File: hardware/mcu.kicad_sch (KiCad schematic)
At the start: 19 parts, among them J1 Micro_SD_Card, J3 USB_C_Receptacle_USB2.0_14P, Q1 Q_NPN_BEC, Q2 Q_NPN_BEC, U1 ESP32-S3-WROOM-1, U6 CH340G

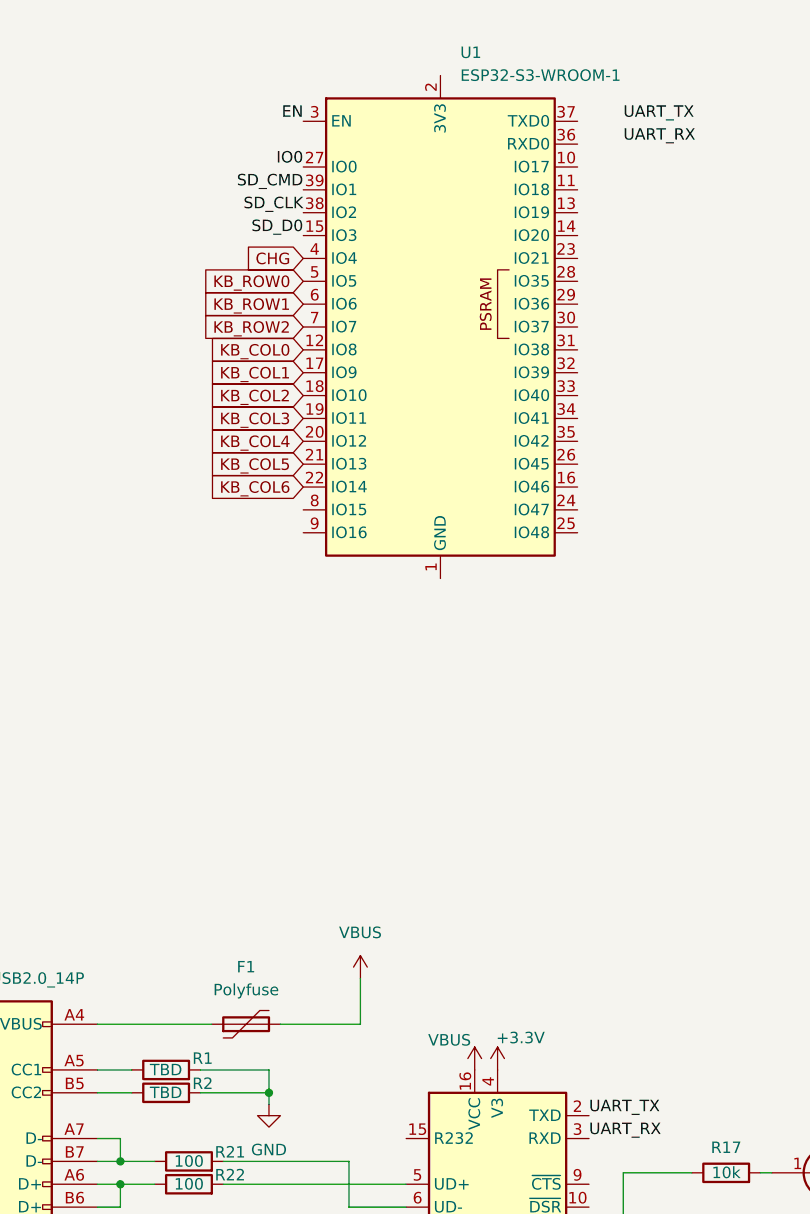
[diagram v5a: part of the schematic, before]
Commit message: rename power symbols, power switch on EN pin instead of VIN
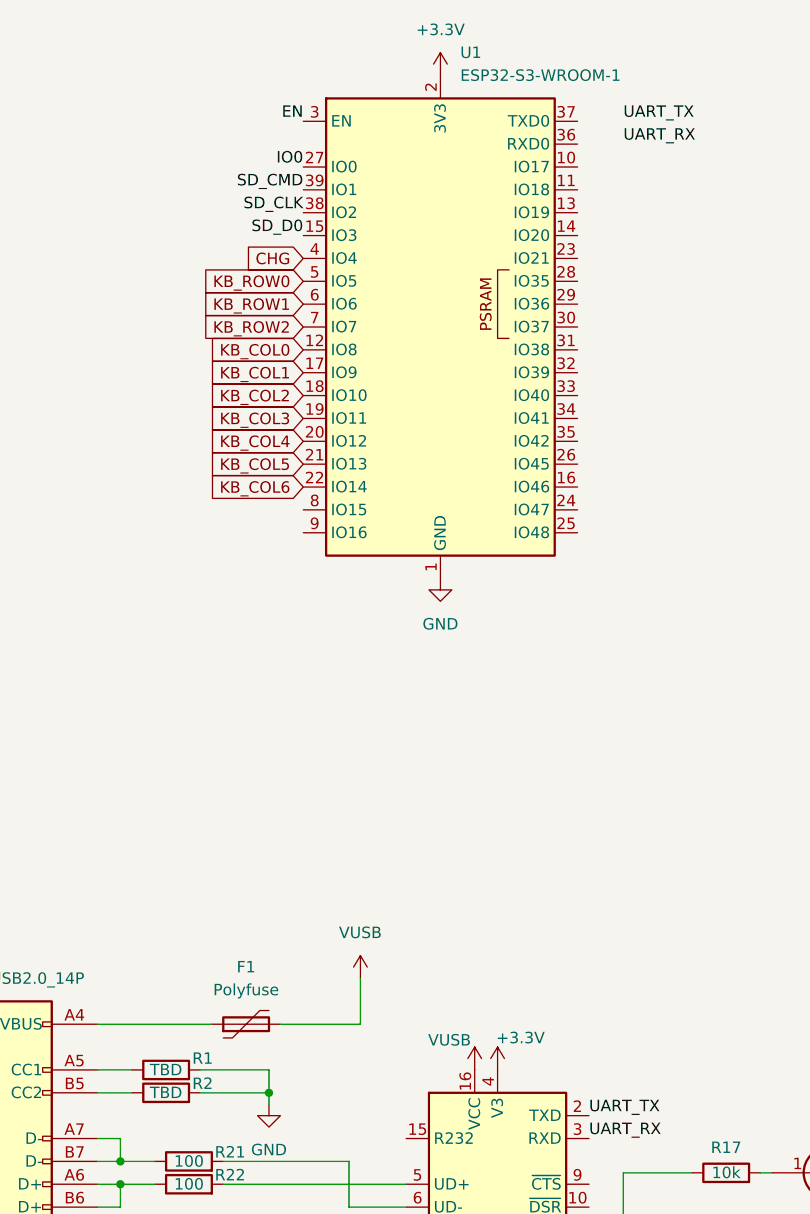
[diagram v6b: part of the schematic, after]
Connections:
- net +3.3V: now also U1.2 (3V3)
- net GND: now also U1.1 (GND), U1.40 (GND), U1.41 (GND)
- net VBUS renamed VUSB
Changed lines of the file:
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@@
+	)
+	(symbol
+		(lib_id "power:+3.3V")
+		(at 86.36 38.1 0)
+		(unit 1)
+		(exclude_from_sim no)
+		(in_bom yes)
+		(on_board yes)
+		(dnp no)
+		(fields_autoplaced yes)
+		(property "Reference" "#PWR045"
+			(at 86.36 41.91 0)
+			(effects
+				(font
+					(size 1.27 1.27)
+				)
+				(hide yes)
+			)
+		)
+		(property "Value" "+3.3V"
+			(at 86.36 33.02 0)
+			(effects
+				(font
+					(size 1.27 1.27)
+				)
+			)
+		)
+		(property "Footprint" ""
+			(at 86.36 38.1 0)
+			(effects
+				(font
+					(size 1.27 1.27)
+				)
+				(hide yes)
+			)
+		)
+		(property "Datasheet" ""
+			(at 86.36 38.1 0)
+			(effects
+				(font
+					(size 1.27 1.27)
+				)
+				(hide yes)
+			)
+		)
+		(property "Description" "Power symbol creates a global label with name \"+3.3V\""
+			(at 86.36 38.1 0)
+			(effects
+				(font
+					(size 1.27 1.27)
+				)
+				(hide yes)
+			)
+		)
+		(pin "1"
+		)
+		(instances
+			(project "badge"
+				(path "/dc4a3d77-b0f8-4e90-a4be-3e93c7025348/d3fb9833-a00e-444d-9e5a-c108fd26b22a"
+					(reference "#PWR045")
+					(unit 1)
+				)
+			)
+		)
 	)
 	(symbol
@@
 			)
 		)
-		(property "Value" "VBUS"
+		(property "Value" "VUSB"
 			(at 87.376 145.288 0)
 			(effects
@@
 			)
 		)
-		(property "Value" "VBUS"
+		(property "Value" "VUSB"
 			(at 77.47 133.35 0)
 			(effects
@@
 					(unit 1)
 				)
+			)
+		)
+	)
+	(symbol
+		(lib_id "power:GND")
+		(at 86.36 93.98 0)
+		(unit 1)
+		(exclude_from_sim no)
+		(in_bom yes)
+		(on_board yes)
+		(dnp no)
+		(fields_autoplaced yes)
+		(property "Reference" "#PWR046"
+			(at 86.36 100.33 0)
+			(effects
+				(font
+					(size 1.27 1.27)
+				)
+				(hide yes)
+			)
+		)
+		(property "Value" "GND"
+			(at 86.36 99.06 0)
+			(effects
+				(font
+					(size 1.27 1.27)
+				)
+			)
+		)
+		(property "Footprint" ""
+			(at 86.36 93.98 0)
+			(effects
+				(font
+					(size 1.27 1.27)
+				)
+				(hide yes)
+			)
+		)
+		(property "Datasheet" ""
+			(at 86.36 93.98 0)
+			(effects
+				(font
+					(size 1.27 1.27)
+				)
+				(hide yes)
+			)
+		)
+		(property "Description" "Power symbol creates a global label with name \"GND\" , ground"
+			(at 86.36 93.98 0)
+			(effects
+				(font
+					(size 1.27 1.27)
+				)
+				(hide yes)
+			)
+		)
+		(pin "1"
+		)
+		(instances
+			(project "badge"
+				(path "/dc4a3d77-b0f8-4e90-a4be-3e93c7025348/d3fb9833-a00e-444d-9e5a-c108fd26b22a"
+					(reference "#PWR046")
+					(unit 1)
+				)

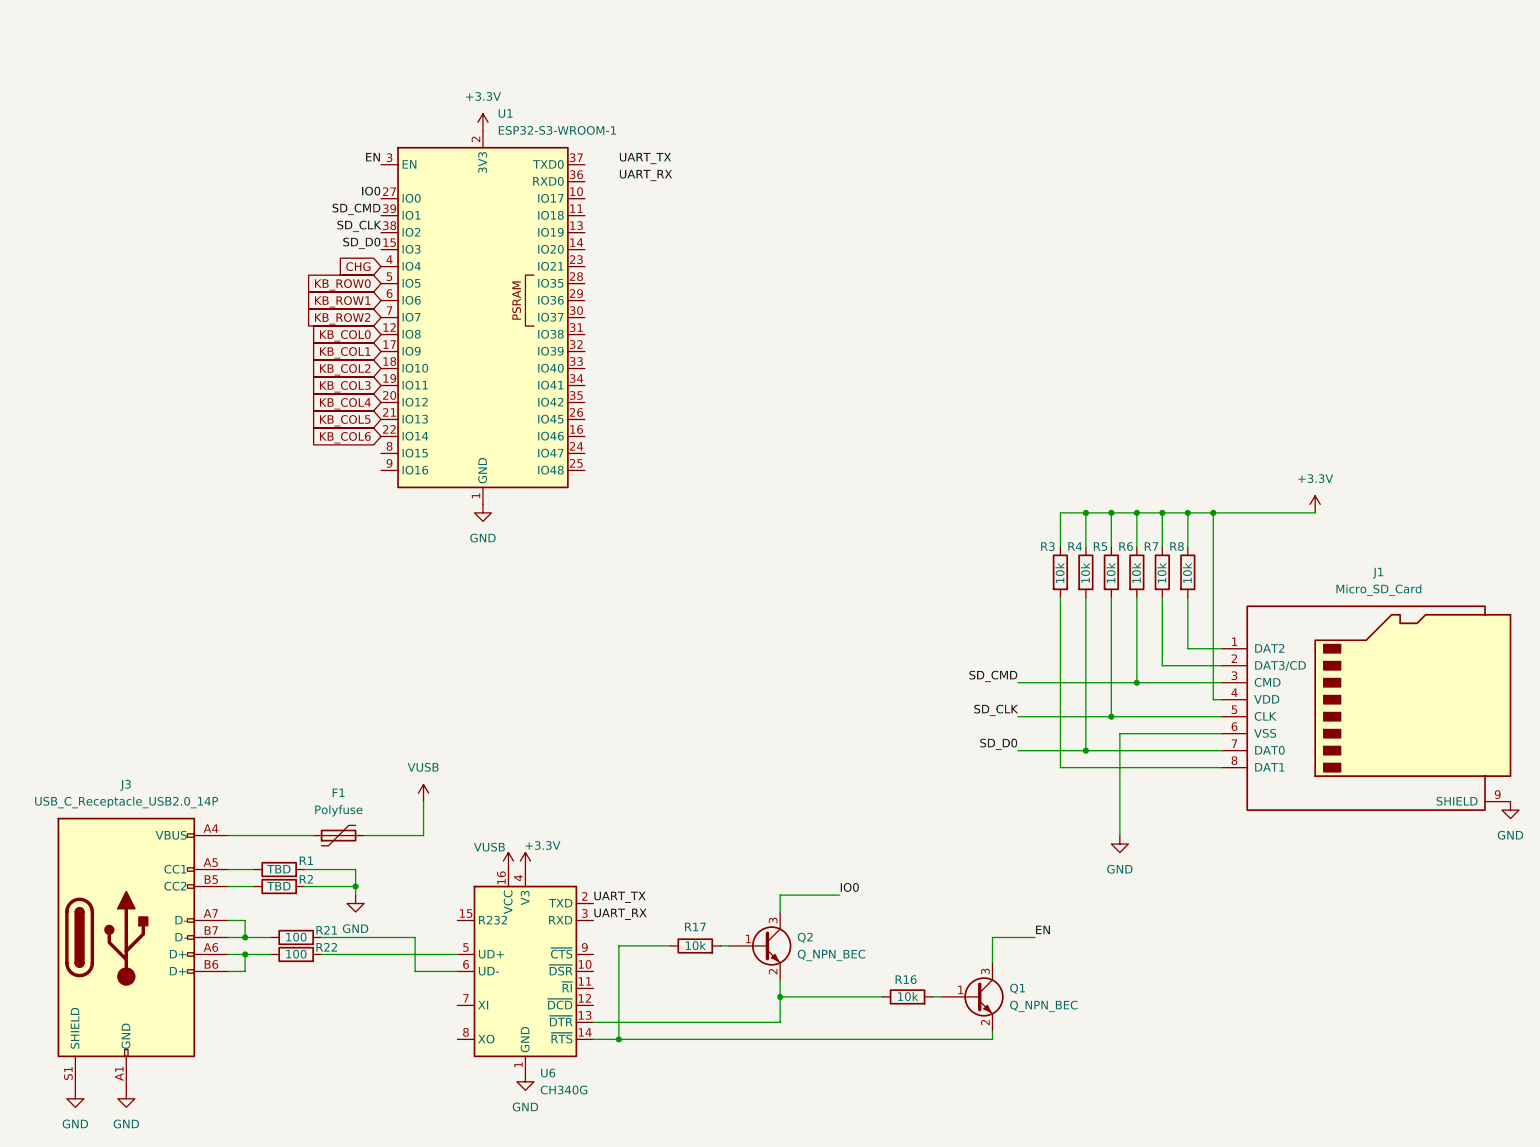
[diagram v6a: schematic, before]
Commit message: remove ch340
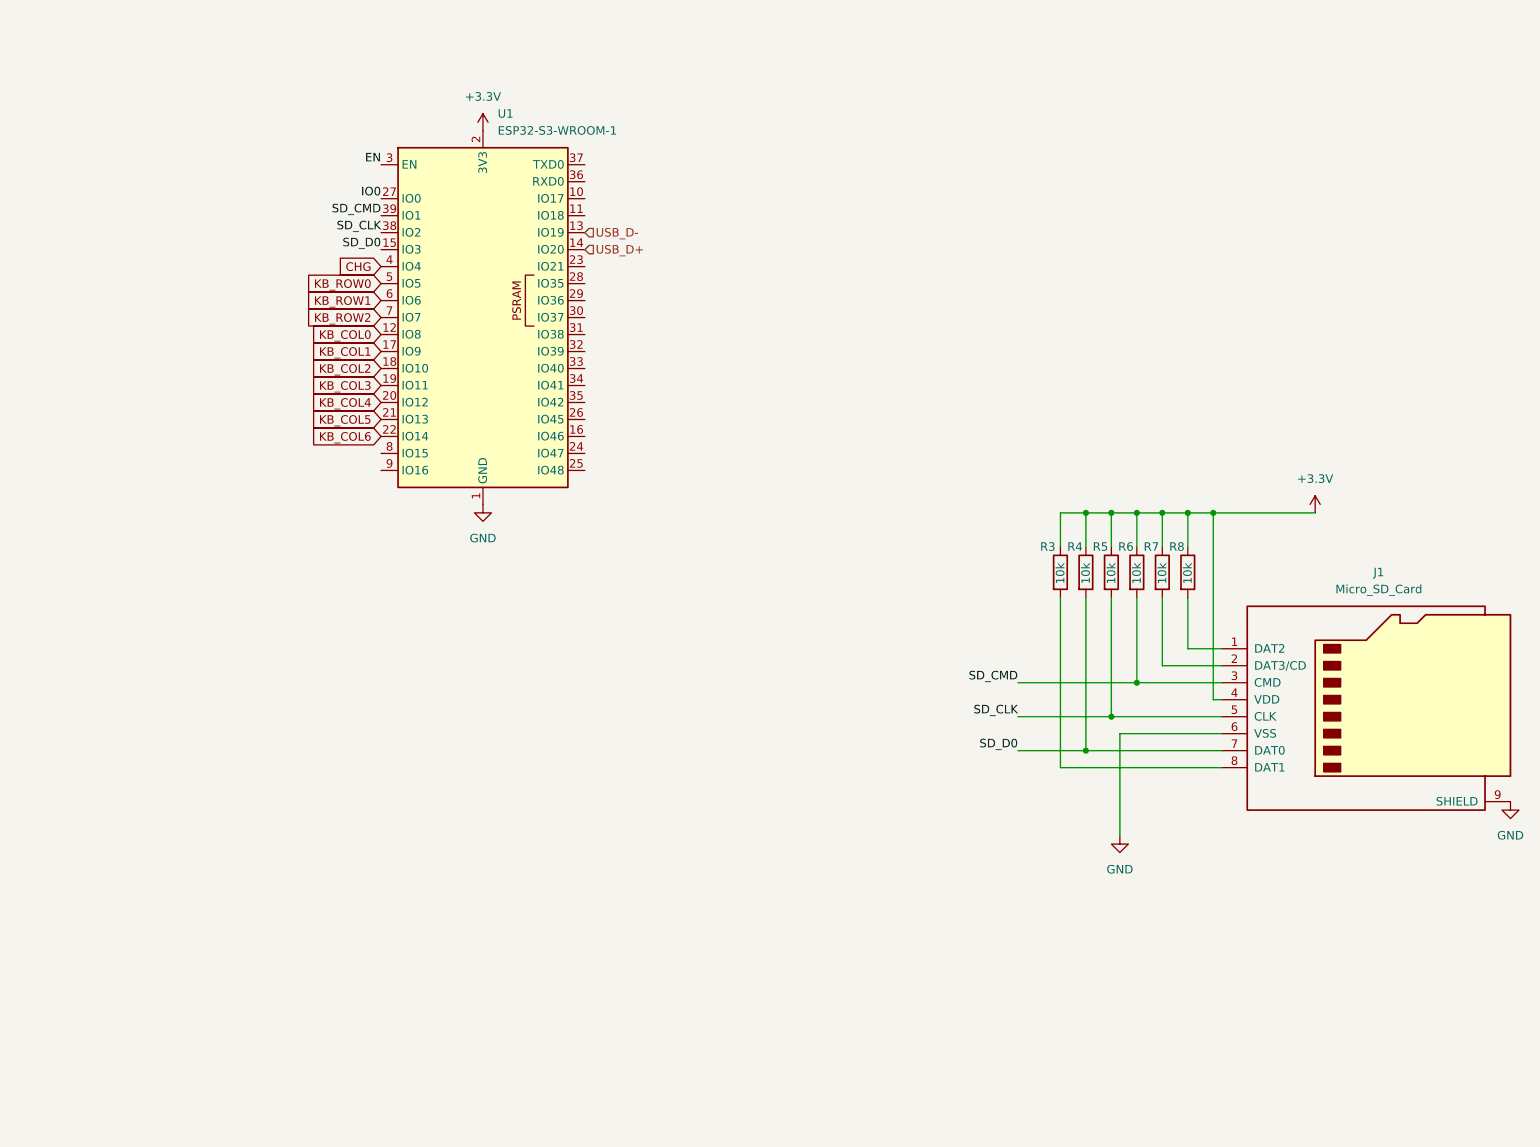
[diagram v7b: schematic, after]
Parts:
- removed F1: Polyfuse, symbol Device:Polyfuse
- removed J3: USB_C_Receptacle_USB2.0_14P, Connector_USB:USB_C_Receptacle_GCT_USB4105-xx-A_16P_TopMnt_Horizontal, symbol Connector:USB_C_Receptacle_USB2.0_14P
- removed Q1, Q2: Q_NPN_BEC, symbol Device:Q_NPN_BEC
- removed R1, R2: TBD, Resistor_SMD:R_0201_0603Metric, symbol Device:R
- removed R16, R17: 10k, symbol Device:R
- removed R21, R22: 100, Resistor_SMD:R_0201_0603Metric, symbol Device:R
- removed U6: CH340G, Package_SO:SOIC-16_3.9x9.9mm_P1.27mm, symbol Interface_USB:CH340G
- R3, R4, R5, R6, R7, R8: footprint Resistor_SMD:R_0201_0603Metric -> Resistor_SMD:R_0603_1608Metric
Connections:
- net USB_D-: now reaches U1.13 (IO19)
- net USB_D+: now reaches U1.14 (IO20)

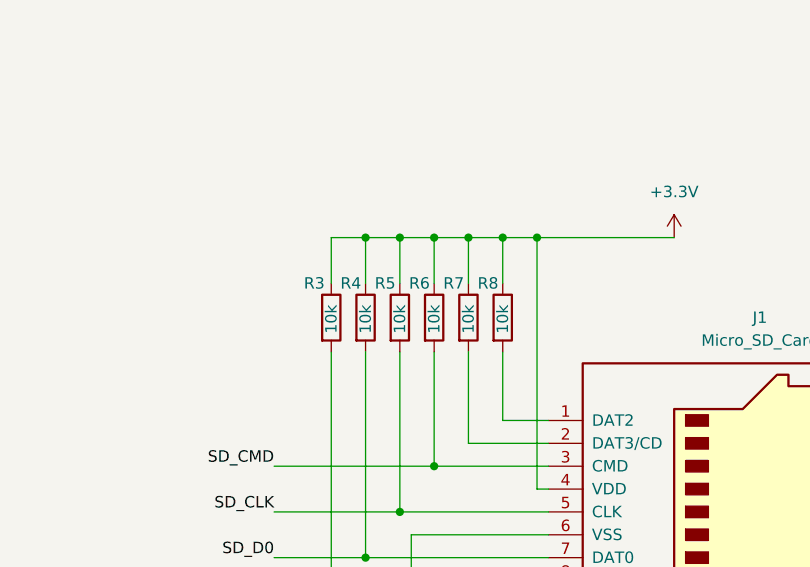
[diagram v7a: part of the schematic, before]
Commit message: update usb port, esd, lcsc
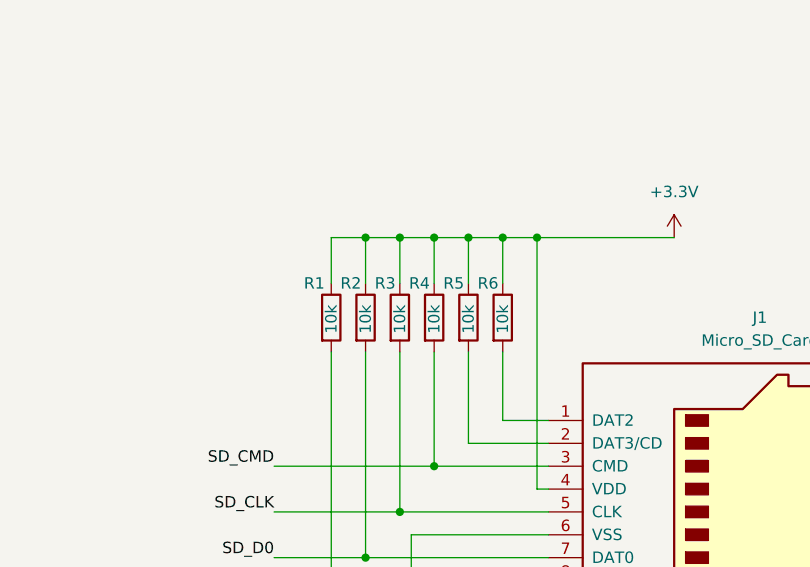
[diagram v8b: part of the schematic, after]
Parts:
- renumbered R3 to R1, R4 to R2, R5 to R3, R6 to R4, R7 to R5, R8 to R6
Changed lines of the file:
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@@
 		(dnp no)
 		(fields_autoplaced yes)
-		(property "Reference" "R3"
+		(property "Reference" "R1"
 			(at 169.672 100.33 0)
 			(effects
@@
 			(project "badge"
 				(path "/dc4a3d77-b0f8-4e90-a4be-3e93c7025348/d3fb9833-a00e-444d-9e5a-c108fd26b22a"
-					(reference "R3")
+					(reference "R1")
 					(unit 1)
 				)
@@
 		(dnp no)
 		(fields_autoplaced yes)
-		(property "Reference" "#PWR07"
+		(property "Reference" "#PWR05"
 			(at 240.03 144.78 0)
 			(effects
@@
 			(project "badge"
 				(path "/dc4a3d77-b0f8-4e90-a4be-3e93c7025348/d3fb9833-a00e-444d-9e5a-c108fd26b22a"
-					(reference "#PWR07")
+					(reference "#PWR05")
 					(unit 1)
 				)
@@
 		(dnp no)
 		(fields_autoplaced yes)
-		(property "Reference" "#PWR045"
+		(property "Reference" "#PWR01"
 			(at 86.36 41.91 0)
 			(effects
@@
 			(project "badge"
 				(path "/dc4a3d77-b0f8-4e90-a4be-3e93c7025348/d3fb9833-a00e-444d-9e5a-c108fd26b22a"
-					(reference "#PWR045")
+					(reference "#PWR01")
 					(unit 1)
 				)
@@
 		(dnp no)
 		(fields_autoplaced yes)
-		(property "Reference" "R4"
+		(property "Reference" "R2"
 			(at 173.736 100.33 0)
 			(effects
@@
 			(project "badge"
 				(path "/dc4a3d77-b0f8-4e90-a4be-3e93c7025348/d3fb9833-a00e-444d-9e5a-c108fd26b22a"
-					(reference "R4")
+					(reference "R2")
 					(unit 1)
 				)
@@
 		(dnp no)
 		(fields_autoplaced yes)
-		(property "Reference" "#PWR06"
+		(property "Reference" "#PWR03"
 			(at 181.61 149.86 0)
 			(effects
@@
 			(project "badge"
 				(path "/dc4a3d77-b0f8-4e90-a4be-3e93c7025348/d3fb9833-a00e-444d-9e5a-c108fd26b22a"
-					(reference "#PWR06")
+					(reference "#PWR03")
 					(unit 1)
 				)
@@
 		(dnp no)
 		(fields_autoplaced yes)
-		(property "Reference" "R8"
+		(property "Reference" "R6"
 			(at 188.976 100.33 0)
 			(effects
@@
 			(project "badge"
 				(path "/dc4a3d77-b0f8-4e90-a4be-3e93c7025348/d3fb9833-a00e-444d-9e5a-c108fd26b22a"
-					(reference "R8")
+					(reference "R6")
 					(unit 1)
 				)
@@
 		(dnp no)
 		(fields_autoplaced yes)
-		(property "Reference" "R7"
+		(property "Reference" "R5"
 			(at 185.166 100.33 0)
 			(effects
@@
 			(project "badge"
 				(path "/dc4a3d77-b0f8-4e90-a4be-3e93c7025348/d3fb9833-a00e-444d-9e5a-c108fd26b22a"
-					(reference "R7")
+					(reference "R5")
 					(unit 1)
 				)
@@
 		(dnp no)
 		(fields_autoplaced yes)
-		(property "Reference" "R5"
+		(property "Reference" "R3"
 			(at 177.546 100.33 0)
 			(effects
@@
 			(project "badge"
 				(path "/dc4a3d77-b0f8-4e90-a4be-3e93c7025348/d3fb9833-a00e-444d-9e5a-c108fd26b22a"
-					(reference "R5")
+					(reference "R3")
 					(unit 1)
 				)
@@
 		(dnp no)
 		(fields_autoplaced yes)
-		(property "Reference" "R6"
+		(property "Reference" "R4"
 			(at 181.356 100.33 0)
 			(effects
@@
 			(project "badge"
 				(path "/dc4a3d77-b0f8-4e90-a4be-3e93c7025348/d3fb9833-a00e-444d-9e5a-c108fd26b22a"
-					(reference "R6")
+					(reference "R4")
 					(unit 1)
 				)
@@
 		(dnp no)
 		(fields_autoplaced yes)
-		(property "Reference" "#PWR05"
+		(property "Reference" "#PWR04"
 			(at 210.82 99.06 0)
 			(effects
@@
 			(project "badge"
 				(path "/dc4a3d77-b0f8-4e90-a4be-3e93c7025348/d3fb9833-a00e-444d-9e5a-c108fd26b22a"
-					(reference "#PWR05")
+					(reference "#PWR04")
 					(unit 1)
 				)
@@
 		(dnp no)
 		(fields_autoplaced yes)
-		(property "Reference" "#PWR046"
+		(property "Reference" "#PWR02"
 			(at 86.36 100.33 0)
 			(effects
@@
 			(project "badge"
 				(path "/dc4a3d77-b0f8-4e90-a4be-3e93c7025348/d3fb9833-a00e-444d-9e5a-c108fd26b22a"
-					(reference "#PWR046")
-					(unit 1)
-				)
+					(reference "#PWR02")
+					(unit 1)
+				)
